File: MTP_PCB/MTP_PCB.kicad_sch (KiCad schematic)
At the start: 17 parts, among them J1 GPIO, J2 USB_A, J3 Conn_01x03, SW1 SW_DPDT_x2, SW2 SW_DPDT_x2, SW3 SW_DPDT_x2, SW4 SW_DIP_x01, SW6 SW_DIP_x01, U1 NRF24L01_Breakout

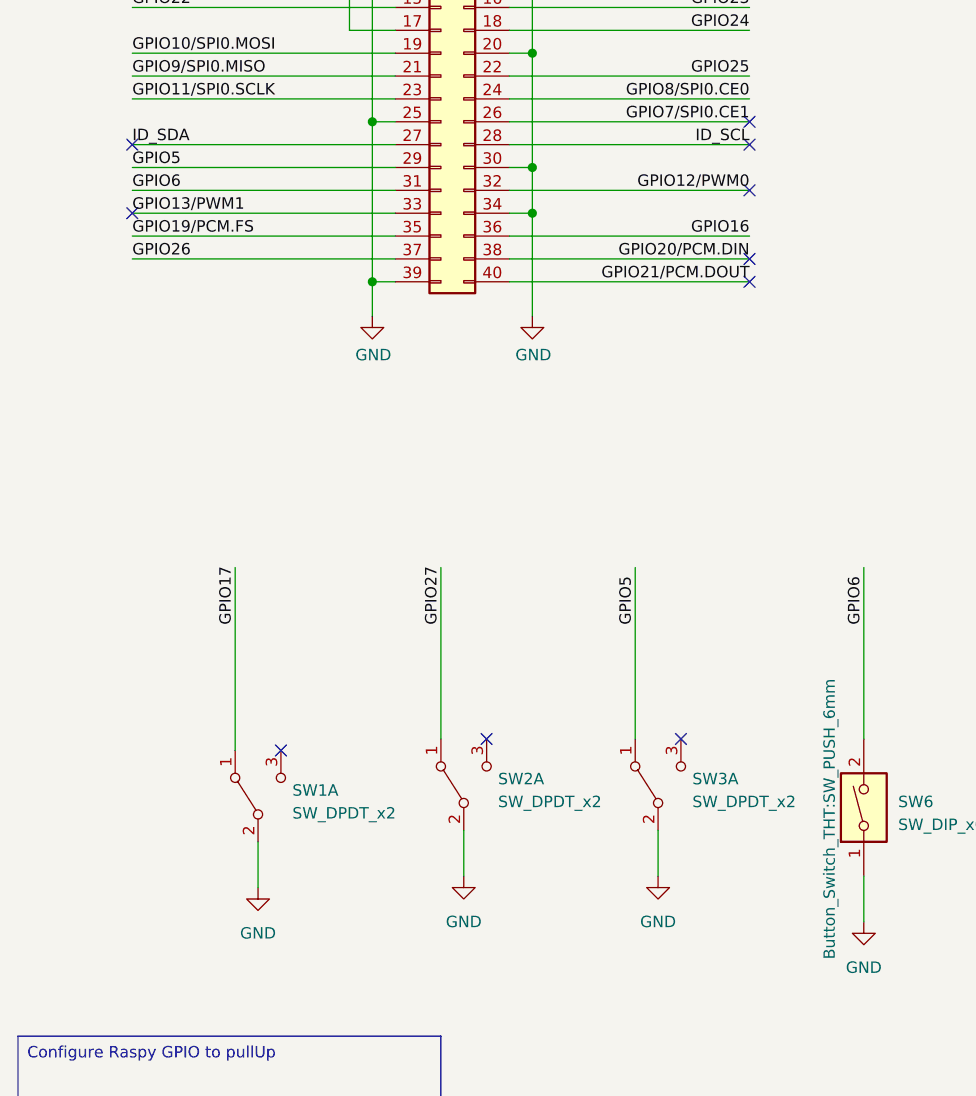
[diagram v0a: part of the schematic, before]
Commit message: remove GND planes
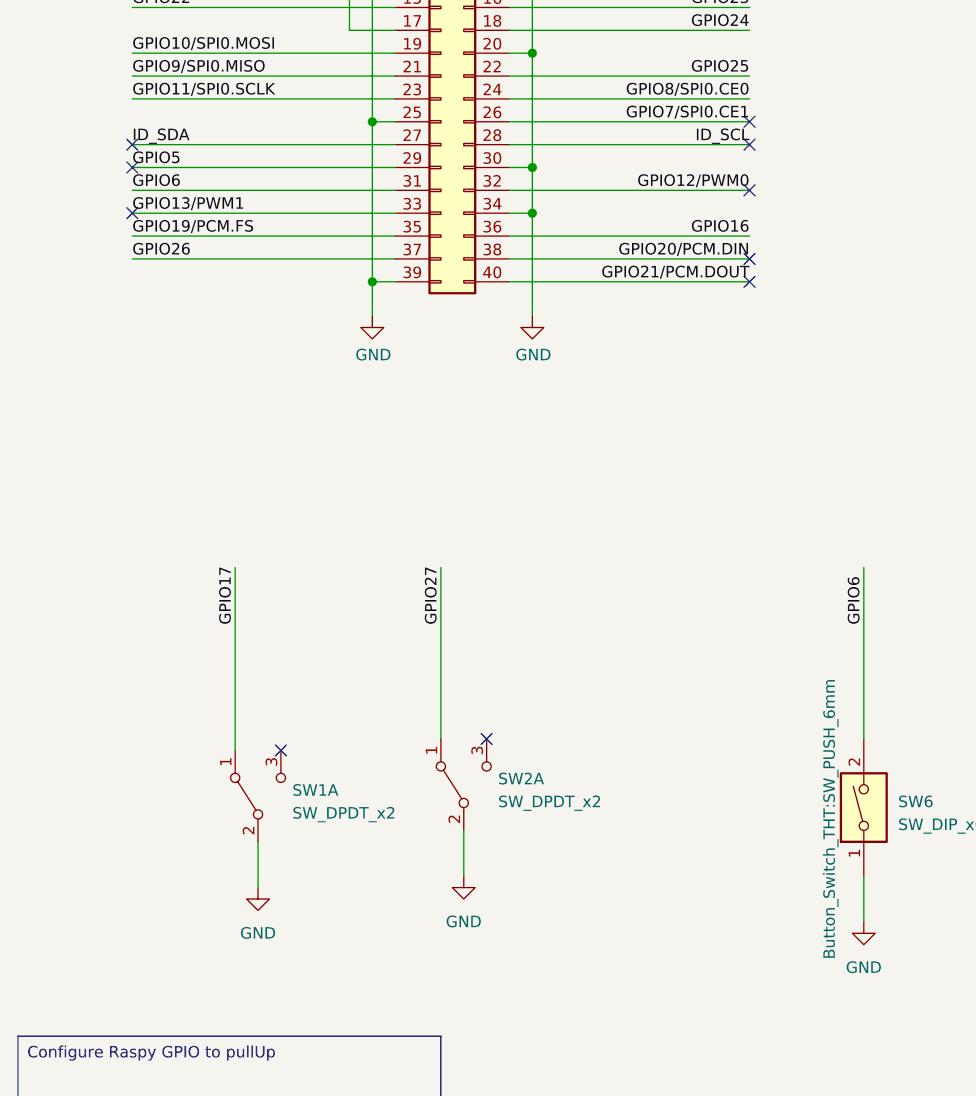
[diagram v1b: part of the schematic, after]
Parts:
- removed SW3: SW_DPDT_x2, MMS_footprints:SW_MTS102_3Pins_2Positions, symbol Switch:SW_DPDT_x2
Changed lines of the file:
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@@
   (no_connect (at 48.26 128.27))
   (no_connect (at 100.33 60.96))
-  (no_connect (at 92.71 127))
   (no_connect (at 100.33 38.1))
   (no_connect (at 31.75 33.02))
+  (no_connect (at 31.75 63.5))
   (no_connect (at 31.75 68.58))
   (no_connect (at 100.33 76.2))
@@
     (stroke (width 0) (type solid))
   )
-  (wire (pts (xy 87.63 107.95) (xy 87.63 127))
-    (stroke (width 0) (type default))
-  )
   (wire (pts (xy 180.34 40.64) (xy 180.34 52.07))
     (stroke (width 0) (type default))
@@
   (wire (pts (xy 31.75 55.88) (xy 60.96 55.88))
     (stroke (width 0) (type solid))
-  )
-  (wire (pts (xy 90.17 137.16) (xy 90.17 142.24))
-    (stroke (width 0) (type default))
   )
   (wire (pts (xy 203.2 52.07) (xy 219.71 52.07))
@@
   (text "NRF25L01\n" (at 220.98 29.21 0)
     (effects (font (size 4 4)) (justify left bottom))
-  )
-  (label "GPIO5" (at 87.63 114.3 90) (fields_autoplaced)
-    (effects (font (size 1.27 1.27)) (justify left bottom))
   )
   (label "GPIO17" (at 43.18 114.3 90) (fields_autoplaced)
@@
     )
   )
-  (symbol (lib_name "GND_1") (lib_id "power:GND") (at 90.17 142.24 0) (unit 1)
-    (in_bom yes) (on_board yes) (dnp no) (fields_autoplaced)
-    (property "Reference" "#PWR015" (at 90.17 148.59 0)
-      (effects (font (size 1.27 1.27)) hide)
-    )
-    (property "Value" "GND" (at 90.17 147.32 0)
-      (effects (font (size 1.27 1.27)))
-    )
-    (property "Footprint" "" (at 90.17 142.24 0)
-      (effects (font (size 1.27 1.27)) hide)
-    )
-    (property "Datasheet" "" (at 90.17 142.24 0)
-      (effects (font (size 1.27 1.27)) hide)
-    )
-    (pin "1")
-    (instances
-      (project "MTP_PCB"
-        (path "/e63e39d7-6ac0-4ffd-8aa3-1841a4541b55"
-          (reference "#PWR015") (unit 1)
-        )
-      )
-    )
-  )
   (symbol (lib_id "power:+5V") (at 166.37 44.45 0) (unit 1)
     (in_bom yes) (on_board yes) (dnp no)
@@
         )
       )
-    )
-  )
-  (symbol (lib_id "Switch:SW_DPDT_x2") (at 90.17 132.08 90) (unit 1)
-    (in_bom yes) (on_board yes) (dnp no) (fields_autoplaced)
-    (property "Reference" "SW3" (at 93.98 131.445 90)
-      (effects (font (size 1.27 1.27)) (justify right))
-    )
-    (property "Value" "SW_DPDT_x2" (at 93.98 133.985 90)
-      (effects (font (size 1.27 1.27)) (justify right))
-    )
-    (property "Footprint" "MMS_footprints:SW_MTS102_3Pins_2Positions" (at 90.17 132.08 0)
-      (effects (font (size 1.27 1.27)) hide)
-    )
-    (property "Datasheet" "~" (at 90.17 132.08 0)
-      (effects (font (size 1.27 1.27)) hide)
-    )
-    (pin "1")
-    (pin "2")
-    (pin "3")
-    (pin "4")
-    (pin "5")
-    (pin "6")
-    (instances
-      (project "MTP_PCB"
-        (path "/e63e39d7-6ac0-4ffd-8aa3-1841a4541b55"
-          (reference "SW3") (unit 1)
-        )
-      )
